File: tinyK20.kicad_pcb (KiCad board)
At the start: 2 copper layers, 22.5 x 52.3 mm, 37 parts, among them CON1 USB-MICRO-B, P1 CONN_01X16, P2 CONN_01X16, P35 CONN_5X2, P38 CONN_5X2, SW1 SW_PUSH, U1 MK20DX128VFT5, U2 LT1129CST-3.3, U4 74AHC1G125, Y1 8MHz, Y2 32.768kHz

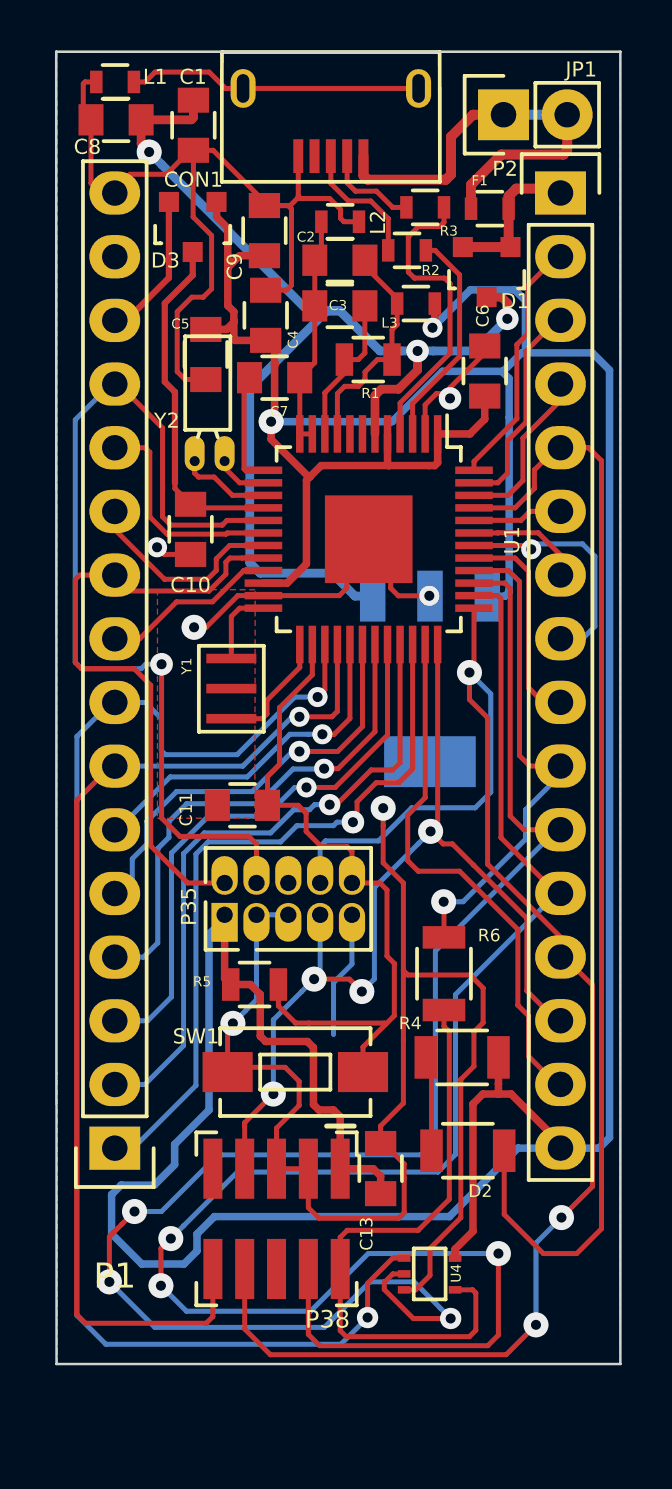
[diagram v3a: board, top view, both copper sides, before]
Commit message: Refresh the project with latest KiCad
Refresh the schematic and reorganize the placement of components adding a plug of nails optional debug port
Redo the PCB playout: round corners, update the footprints with latest available from KiCad libraries, add silk screen lables for header pins
Add a README file with screenshot images of the schematic and PCB layout top and board 3D view
Add some missing 3D files for fuse and pushbutton
Change the 3.3V regulator with a smaller package
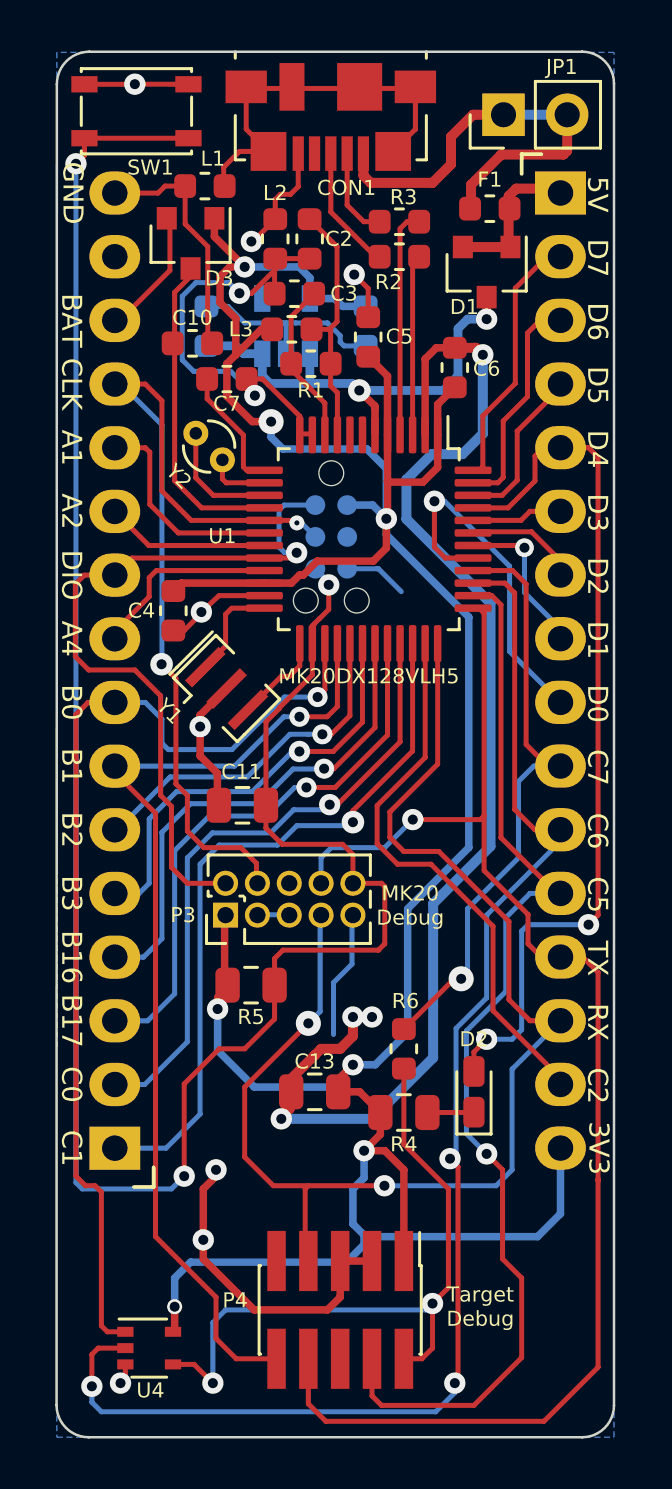
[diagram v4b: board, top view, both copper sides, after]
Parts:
- removed C8: 100n, Capacitors_SMD:C_0805
- removed P35: CONN_5X2, Pin_Headers:Pin_Header_Straight_2x05_Pitch1.27mm
- removed P38: CONN_5X2, Pin_Headers:CONN-2x5-1.27-SMT
- added J2: Conn_02x03_Odd_Even, Connector:Tag-Connect_TC2030-IDC-NL_2x03_P1.27mm_Vertical, B.Cu at (62.3, 41.5)
- added P3: Debug, Connector_PinHeader_1.27mm:PinHeader_2x05_P1.27mm_Vertical, F.Cu at (58.1, 56.6)
- added P4: Conn_02x05_Odd_Even, Connector_PinHeader_1.27mm:PinHeader_2x05_P1.27mm_Vertical_SMD, F.Cu at (62.7, 72.4)
- C1, C9: value 100n -> 10uF; footprint Capacitors_SMD:C_0805 -> Capacitor_SMD:C_0603_1608Metric; moved to B.Cu
- C10, C2, C3, C4, C5, C6, C7: footprint Capacitors_SMD:C_0805 -> Capacitor_SMD:C_0603_1608Metric
- C11, C13: footprint Capacitors_SMD:C_0805 -> Capacitor_SMD:C_0805_2012Metric
- CON1: footprint Connect:USB_Micro-B -> Connector_USB:USB_Micro-B_Molex_47346-0001
- D1, D3: footprint TO_SOT_Packages_SMD:SOT-23 -> Package_TO_SOT_SMD:SOT-23
- D2: footprint Resistors_SMD:R_1206 -> LED_SMD:LED_0603_1608Metric_Castellated
- F1: footprint Resistors_SMD:R_0603 -> Fuse:Fuse_0603_1608Metric
- JP1: footprint Pin_Headers:Pin_Header_Straight_1x02 -> Connector_PinHeader_2.54mm:PinHeader_1x02_P2.54mm_Vertical
- L1, L2, L3: footprint Resistors_SMD:R_0603 -> Inductor_SMD:L_0603_1608Metric
- P1, P2: footprint Pin_Headers:Pin_Header_Straight_1x16 -> my_connectors:Pin_Header_Straight_1x16
- R1: footprint Resistors_SMD:R_0805 -> Resistor_SMD:R_0603_1608Metric
- R2, R3: footprint Resistors_SMD:R_0603 -> Resistor_SMD:R_0603_1608Metric
- R4: value 1k -> 1K; footprint Resistors_SMD:R_1206 -> Resistor_SMD:R_0805_2012Metric
- R5: value 10k -> 10K; footprint Resistors_SMD:R_0805 -> Resistor_SMD:R_0805_2012Metric
- R6: footprint Resistors_SMD:R_1206 -> Resistor_SMD:R_0603_1608Metric
- SW1: footprint Buttons_Switches_SMD:SW_SPST_EVQPE1 -> Button_Switch_SMD:SW_SPST_PTS810
- U1: footprint Housings_QFP:TQFP-48-1EP_7x7mm_Pitch0.5mm -> Package_QFP:LQFP-48_7x7mm_P0.5mm
- U2: value LT1129CST-3.3 -> XC6220B331MR; footprint TO_SOT_Packages_SMD:SOT-223 -> Package_TO_SOT_SMD:SOT-23-5
- U4: footprint TO_SOT_Packages_SMD:SOT-353 -> Package_TO_SOT_SMD:SOT-353_SC-70-5
- Y1: footprint Crystals:CERALOCK-CSTCE8M00G15L99-R0 -> Crystal:Resonator_SMD_muRata_CSTxExxV-3Pin_3.0x1.1mm
- Y2: footprint Crystals:Crystal_Round_Horizontal_2mm -> Crystal:Crystal_DS10_D1.0mm_L4.3mm_Vertical
- moved SW1 38.8 mm to (54.5, 24.5)
- moved U2 15.2 mm to (60.5, 33.1), turned to 90 degrees
- moved C4 12.3 mm to (56.0, 44.5), turned to 270 degrees
- moved U4 11.6 mm to (55.0, 73.9)
- moved C1 8.03 mm to (57.3, 33.1), turned to 90 degrees
- moved C10 7.42 mm to (56.8, 33.8), turned to 0 degrees
- moved C5 6.51 mm to (63.8, 33.6), turned to 90 degrees
- moved C9 5.55 mm to (63.7, 33.1), turned to 270 degrees
- moved L1 5.48 mm to (57.3, 27.5)
- moved L3 5.06 mm to (60.7, 33.2), turned to 180 degrees
- moved C13 4.03 mm to (61.6, 63.7), turned to 180 degrees
- moved R6 3.40 mm to (65.2, 62.0)
- moved R4 3.20 mm to (65.2, 64.5), turned to 0 degrees
- moved L2 2.68 mm to (60.1, 29.6), turned to 270 degrees
- moved D2 2.36 mm to (68.0, 63.7), turned to 90 degrees
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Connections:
- net Net-(P38-Pad2) renamed TGT_SWD_IO
- net Net-(R2-Pad2) renamed /UD+
- net Net-(R3-Pad2) renamed /UD-
- net PTA0 renamed SWD_CLK
- net PTA3 renamed SWD_IO
- U2 pad 3: 3V3 -> Vregin
- Y2 pad 1: Net-(U1-Pad15) -> Net-(U1-Pad14)
- Y2 pad 2: Net-(U1-Pad14) -> Net-(U1-Pad15)
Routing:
- net RESET: track 27.8 -> 86.2 mm, vias 0 -> 3
- net 3V3: track 162.9 -> 125.3 mm, vias 2 -> 7
- net Vregin: track 45.6 -> 18.8 mm, vias 3 -> 2
- net PTC5: track 69.6 -> 43.9 mm, vias 3 -> 1
- net UART1_RX: track 38.6 -> 52.3 mm, vias 4 -> 2
- net PTB0: track 53.9 -> 40.5 mm, vias 2 -> 1
- net PTD4: track 44.8 -> 35.2 mm, vias 0 -> 2
- net Net-(C2-Pad2): track 9.33 -> 18.5 mm, vias 0 -> 2
- net PTC6: track 63.9 -> 55.3 mm
- net GND: track 120.6 -> 112.7 mm, vias 6 -> 12
- net PTD0: track 8.55 -> 13.9 mm, vias 0 -> 1
- net UART1_TX: track 60.9 -> 56.2 mm, vias 3 -> 1
- net PTC7: track 20.0 -> 24.3 mm
- net SWD_IO: track 25.4 -> 29.5 mm, vias 0 -> 1
- net Net-(CON1-Pad6): track 11.8 -> 15.7 mm
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- removed copper zone on F.Cu, net GND
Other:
- board size 22.5 x 52.3 mm -> 22.2 x 55.3 mm
- net class 5VPOWER added: clearance 0.16, trace_width 0.35, via_dia 0.6, via_drill 0.4
- net class Default: via_dia 0.6 -> 0.85
- board text added: "3V3"
- board text added: "5V"
- board text added: "A1"
- board text added: "A2"
- board text added: "A4"
- board text added: "B0"
- board text added: "B1"
- board text added: "B16"
- board text added: "B17"
- board text added: "B2"
- board text added: "B3"
- board text added: "BAT"
- board text added: "C0"
- board text added: "C1"
- board text added: "C2"
- board text added: "C5"
- board text added: "C6"
- board text added: "C7"
- board text added: "CLK"
- board text added: "D0"
- board text added: "D1"
- board text added: "D2"
- board text added: "D3"
- board text added: "D4"
- board text added: "D5"
- board text added: "D6"
- board text added: "D7"
- board text added: "DIO"
- board text added: "GND"
- board text added: "MK20 Debug"
- board text added: "MK20DX128VLH5"
- board text added: "RX"
- board text added: "TX"
- board text added: "Target Debug"
